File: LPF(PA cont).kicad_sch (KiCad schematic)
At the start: 2 parts, among them K1 G5V-1, K2 G5V-1

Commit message: Logical Work
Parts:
- added C64, C72: 82pF, symbol Device:C_Small
- added C65, C73: 56pF, symbol Device:C_Small
- added C66, C74: 220pF, symbol Device:C_Small
- added C67, C75: 100pF, symbol Device:C_Small
- added C68: 230pF, symbol Device:C_Small
- added C69: 170pF, symbol Device:C_Small
- added C70: 680pF, symbol Device:C_Small
- added C71: 330pF, symbol Device:C_Small
- added K3, K4, K5, K6, K7, K8: G5V-1, Relay_THT:Relay_SPDT_Omron_G5V-1, symbol Relay:G5V-1
- added L21, L25: 500nH, symbol Device:L_Ferrite_Small
- added L22, L26: 400nH, symbol Device:L_Ferrite_Small
- added L23, L27: 1.5uH, symbol Device:L_Ferrite_Small
- added L24, L28: 750nH, symbol Device:L_Ferrite_Small
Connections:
- net GND: now reaches K2.1
- net GND: now also K1.1, C64.2, C65.2, C66.2, C67.2, C68.2, C69.2, C70.2, C71.2, C72.2, C73.2, C74.2, C75.2, K3.1, K4.1, K5.1, K6.1, K7.1, K8.1
- net LPF_IN: now reaches K2.10
- net LPF_IN: now also K1.10, K3.10, K4.10
- net at K2.5, K2.6: now also C67.1, L24.1
- net at K1.5, K1.6: now also C66.1, L23.1
- new net: C75.1, K6.5, K6.6, L28.2
- new net: C74.1, K5.5, K5.6, L27.2
- new net: C71.1, L24.2, L28.1
- new net: C70.1, L23.2, L27.1
- new net: C69.1, L22.2, L26.1
- new net: C73.1, K8.5, K8.6, L26.2
- new net: C64.1, K3.5, K3.6, L21.1
- new net: C68.1, L21.2, L25.1
- new net: C72.1, K7.5, K7.6, L25.2
- new net: C65.1, K4.5, K4.6, L22.1
- new net LPF_OUT: K5.10, K6.10, K7.10, K8.10
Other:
- note added: "12m-10m"
- note added: "17m-15m"
- note added: "30m-20m"
- note added: "40m"

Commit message: Logical Work, Mixers II
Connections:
- net LPF_IN renamed LPF
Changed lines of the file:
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@@
+		)
+	)
+	(global_label "LPF"
+		(shape input)
+		(at 69.85 35.56 90)
+		(fields_autoplaced yes)
+		(effects
+			(font
+				(size 0.8 0.8)
+			)
+			(justify left)
+		)
+		(property "Intersheetrefs" "${INTERSHEET_REFS}"
+			(at 69.85 31.5464 90)
+			(effects
+				(font
+					(size 1.27 1.27)
+				)
+				(justify left)
+				(hide yes)
+			)
 		)
 	)
@@
 					(unit 1)
 				)
-			)
-		)
-	)
-	(symbol
-		(lib_id "power:+12V")
-		(at 69.85 35.56 0)
-		(unit 1)
-		(exclude_from_sim no)
-		(in_bom yes)
-		(on_board yes)
-		(dnp no)
-		(property "Reference" "#PWR0109"
-			(at 69.85 39.37 0)
-			(effects
-				(font
-					(size 1.27 1.27)
-				)
-				(hide yes)
-			)
-		)
-		(property "Value" "LPF_IN"
-			(at 61.214 34.544 0)
-			(effects
-				(font
-					(size 1.27 1.27)
-				)
-				(justify left)
-			)
-		)
-		(property "Footprint" ""
-			(at 69.85 35.56 0)
-			(effects
-				(font
-					(size 1.27 1.27)
-				)
-				(hide yes)
-			)
-		)
-		(property "Datasheet" ""
-			(at 69.85 35.56 0)
-			(effects
-				(font
-					(size 1.27 1.27)
-				)
-				(hide yes)
-			)
-		)
-		(property "Description" "Power symbol creates a global label with name \"+12V\""
-			(at 69.85 35.56 0)
-			(effects
-				(font
-					(size 1.27 1.27)
-				)
-				(hide yes)
-			)
-		)
-		(pin "1"
-		)
-		(instances
-			(project "Omega Radio"
-				(path "/3468ce30-82a7-4087-a7ac-02063723d842/22f96ef4-9360-4557-9cd6-28177b6e1de3"
-					(reference "#PWR0109")
-					(unit 1)
-				)

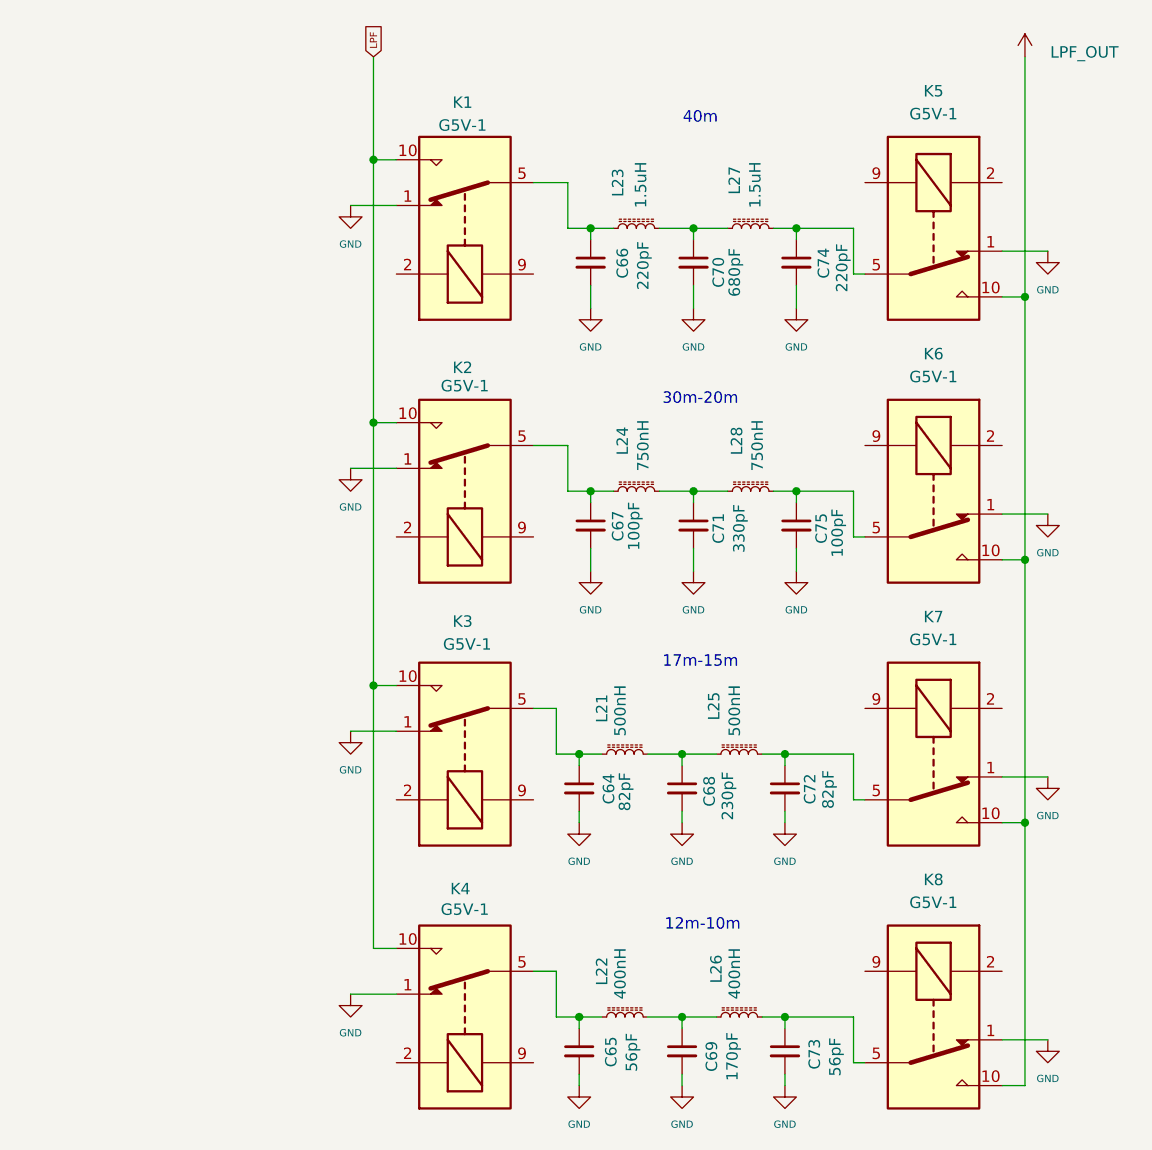
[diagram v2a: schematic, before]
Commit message: Resistive adder of mixers
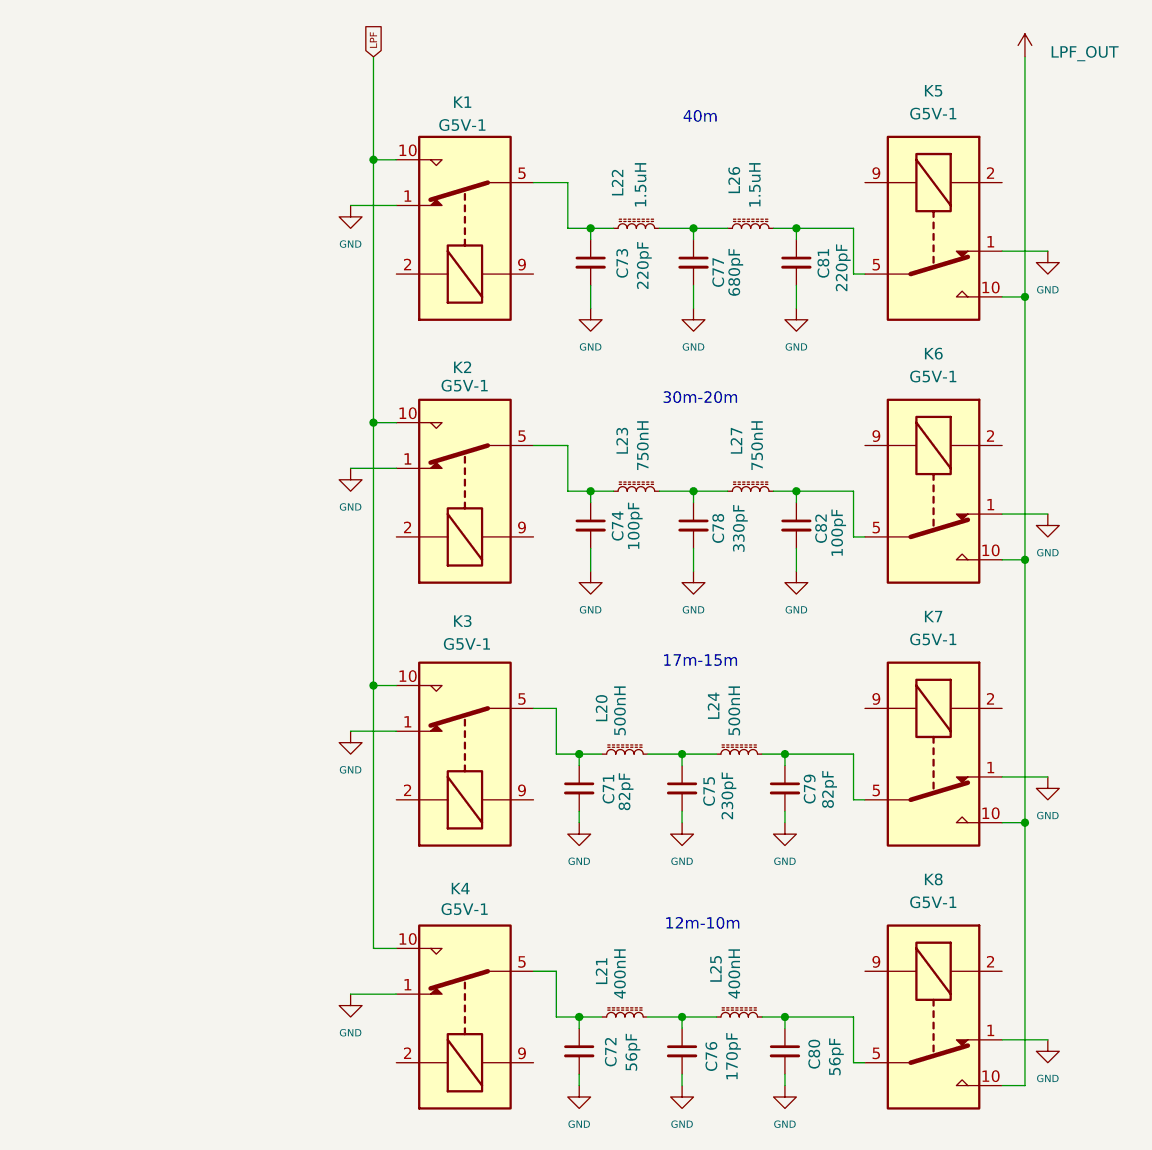
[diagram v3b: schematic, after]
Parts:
- renumbered C64 to C71, C65 to C72, C66 to C73, C67 to C74, C68 to C75, C69 to C76, C70 to C77, C71 to C78, C72 to C79, C73 to C80, C74 to C81, C75 to C82, L21 to L20, L22 to L21, L23 to L22, L24 to L23, L25 to L24, L26 to L25, L27 to L26, L28 to L27

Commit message: BPF Work 2
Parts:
- renumbered C71 to C106, C72 to C107, C73 to C108, C74 to C109, C75 to C110, C76 to C111, C77 to C112, C78 to C113, C79 to C114, C80 to C115, C81 to C116, C82 to C117, L20 to L40, L21 to L41, L22 to L42, L23 to L43, L24 to L44, L25 to L45, L26 to L46, L27 to L47

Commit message: BPF Work 3
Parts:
- renumbered C106 to C134, C107 to C135, C108 to C136, C109 to C137, C110 to C138, C111 to C139, C112 to C140, C113 to C141, C114 to C142, C115 to C143, C116 to C144, C117 to C145, L40 to L44, L41 to L45, L42 to L46, L43 to L47, L44 to L48, L45 to L49, L46 to L50, L47 to L51

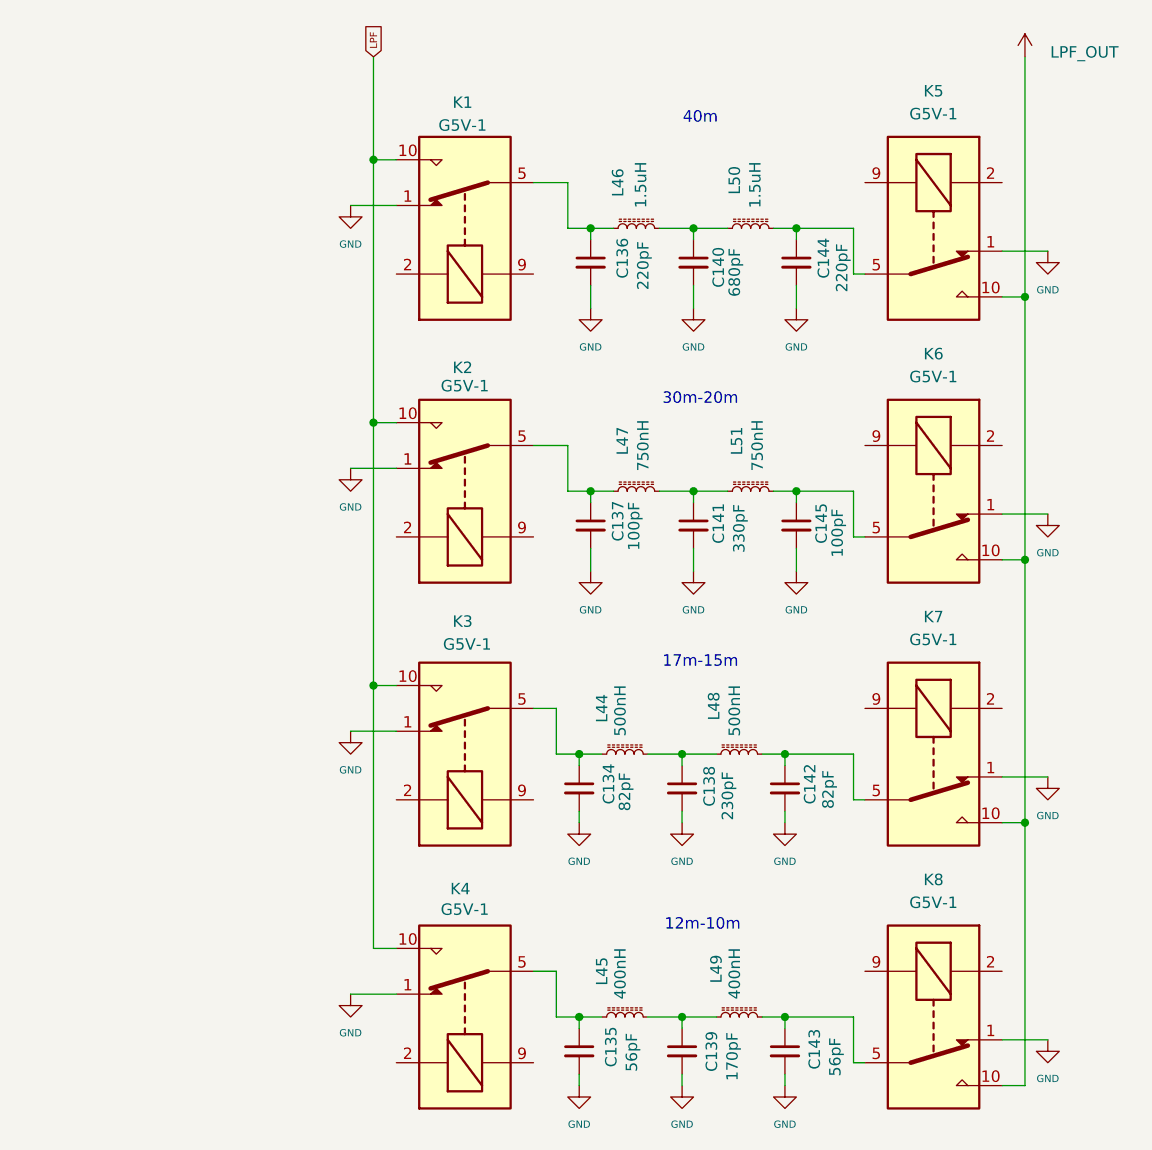
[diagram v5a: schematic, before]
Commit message: Rf RX amplifier, BPF RX
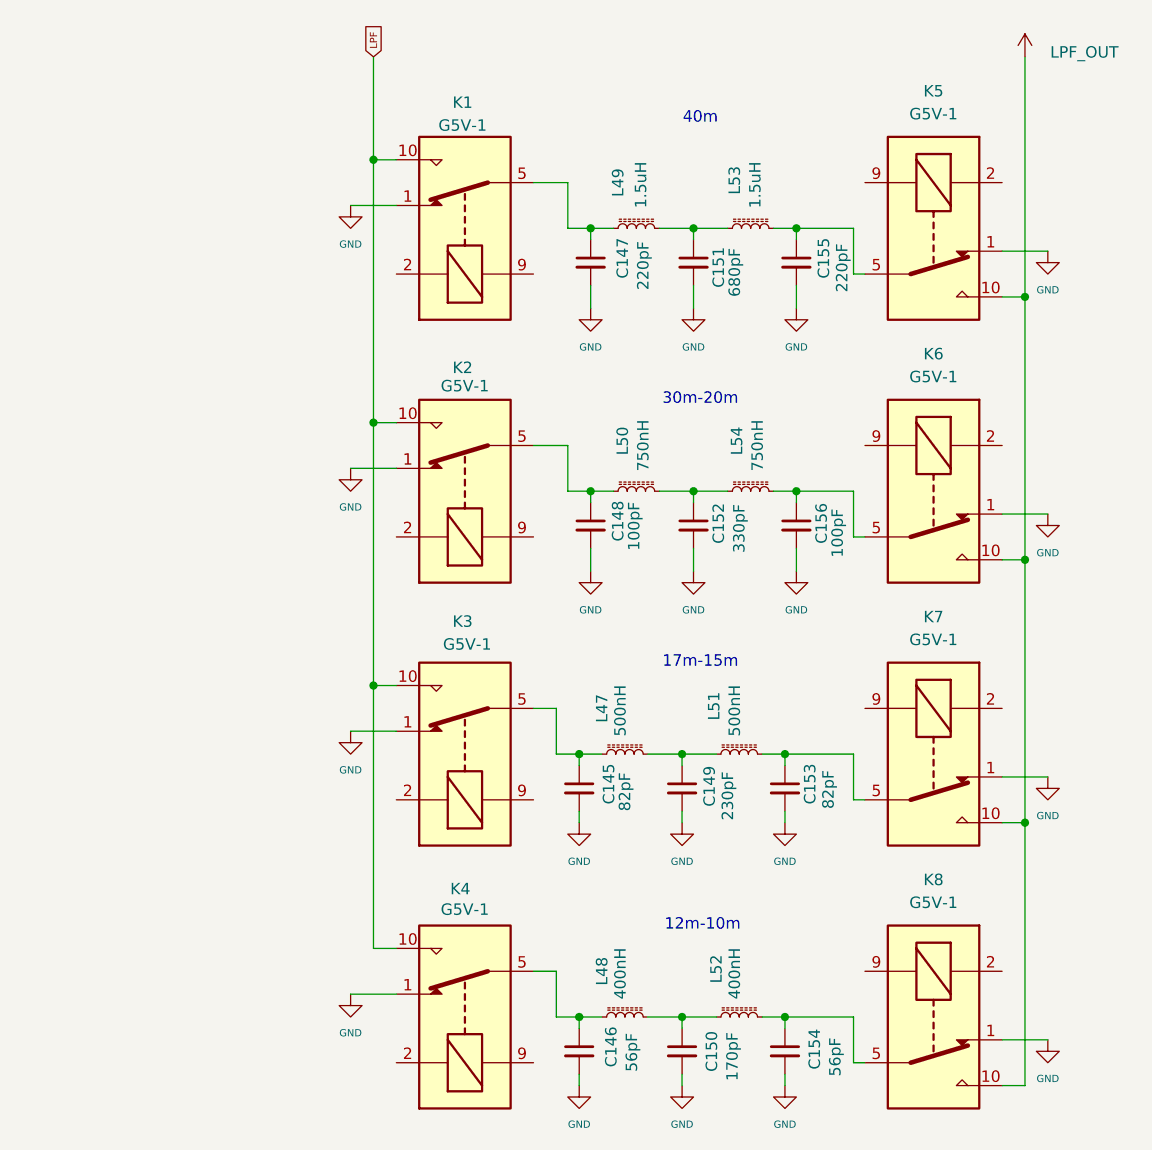
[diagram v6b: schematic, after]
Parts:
- renumbered C134 to C145, C135 to C146, C136 to C147, C137 to C148, C138 to C149, C139 to C150, C140 to C151, C141 to C152, C142 to C153, C143 to C154, C144 to C155, C145 to C156, L44 to L47, L45 to L48, L46 to L49, L47 to L50, L48 to L51, L49 to L52, L50 to L53, L51 to L54

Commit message: RF Gain
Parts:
- renumbered C145 to C150, C146 to C151, C147 to C152, C148 to C153, C149 to C154, C150 to C155, C151 to C156, C152 to C157, C153 to C158, C154 to C159, C155 to C160, C156 to C161

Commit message: AGC Work 4
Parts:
- renumbered C150 to C154, C151 to C155, C152 to C156, C153 to C157, C154 to C158, C155 to C159, C156 to C160, C157 to C161, C158 to C162, C159 to C163, C160 to C164, C161 to C165
